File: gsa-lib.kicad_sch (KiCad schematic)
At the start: 61 parts, among them J1 CONN-1, J2 CONN-2, J3 CONN-4, J4 SKT-2, J5 CONN-3, J6 CONN-5, J7 SKT-3, K1 RELAY-SPDT, K2 RELAY-DPDT, Q1 NPN, Q2 PNP, Q3 NFET, Q4 PFET, Q5 NMOS-D, Q6 PMOS-D, Q7 NMOS-E, Q8 PMOS-E, Q9 UJT, SW1 SW-PUSH, SW2 SW-SPST, SW3 SW-DPST, SW4 SW-DPDT, SW5 SW-SPDT, SW6 SW-SP2T, SW7 SW-SP3T, T1 XFRMR, T2 XFRMR-CTR, T3 XFRMR-DUAL, U1 40106, U10 LM1876, U11 LM78XX, U12 LM79XX, U13 LM317, U14 LM377, U15 TDA2009, U16 NE555, U2 4017, U3 LM386, U4 TBA820M, U5 4093, U6 4066, U7 LM1875, U8 OPAMP, U9 741, X1 LINK

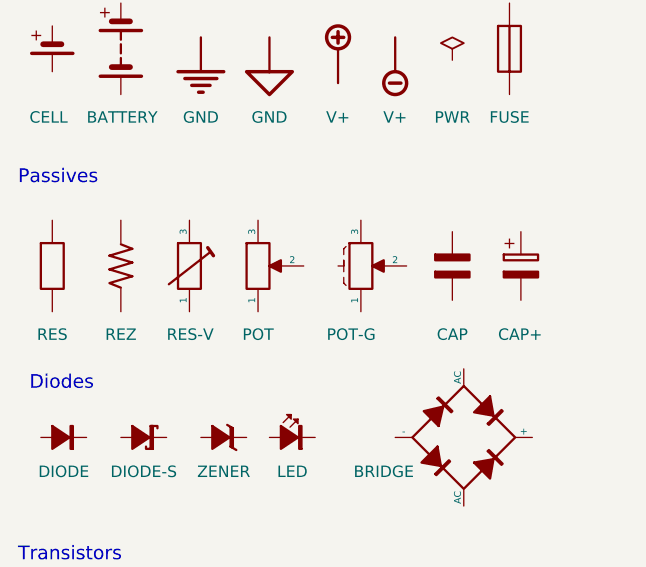
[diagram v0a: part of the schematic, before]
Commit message: KiCad v10 and add RES-V
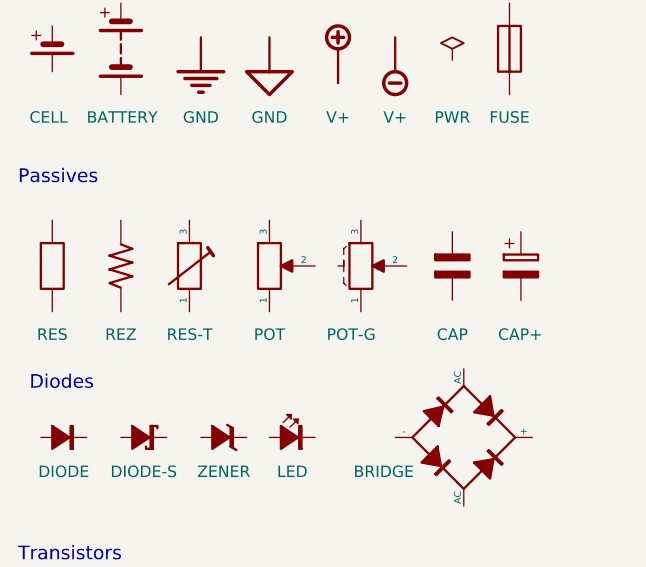
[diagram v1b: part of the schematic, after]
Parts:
- removed VR1: RES-V, symbol gsa:RES-V
- added VR1: RES-T, symbol GSA:RES-T
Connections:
- new net: VR1.2, VR1.3
